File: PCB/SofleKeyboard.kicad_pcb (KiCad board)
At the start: 2 copper layers, 137.2 x 109.2 mm, 87 parts, among them J1 LED, J2 4PIN, J3 OLED, P1 i2c_pin, P2 i2c_pin, SW1 SW_PUSH, SW10 SW_PUSH, SW11 SW_PUSH, SW12 SW_PUSH, SW13 SW_PUSH, SW14 SW_PUSH, SW15 SW_PUSH, SW16 SW_PUSH, SW17 SW_PUSH, SW18 SW_PUSH, SW19 SW_PUSH, SW2 SW_PUSH, SW20 SW_PUSH, SW21 SW_PUSH, SW22 SW_PUSH, SW23 SW_PUSH, SW24 SW_PUSH, SW25 Rotary_Encoder_Switch, SW26 SW_PUSH, SW27 SW_PUSH, SW28 SW_PUSH, SW29 SW_PUSH, SW3 SW_PUSH, SW30 SW_PUSH, SW4 SW_PUSH, SW5 SW_PUSH, SW6 SW_PUSH, SW7 SW_PUSH, SW8 SW_PUSH, SW9 SW_PUSH, U1 ProMicro

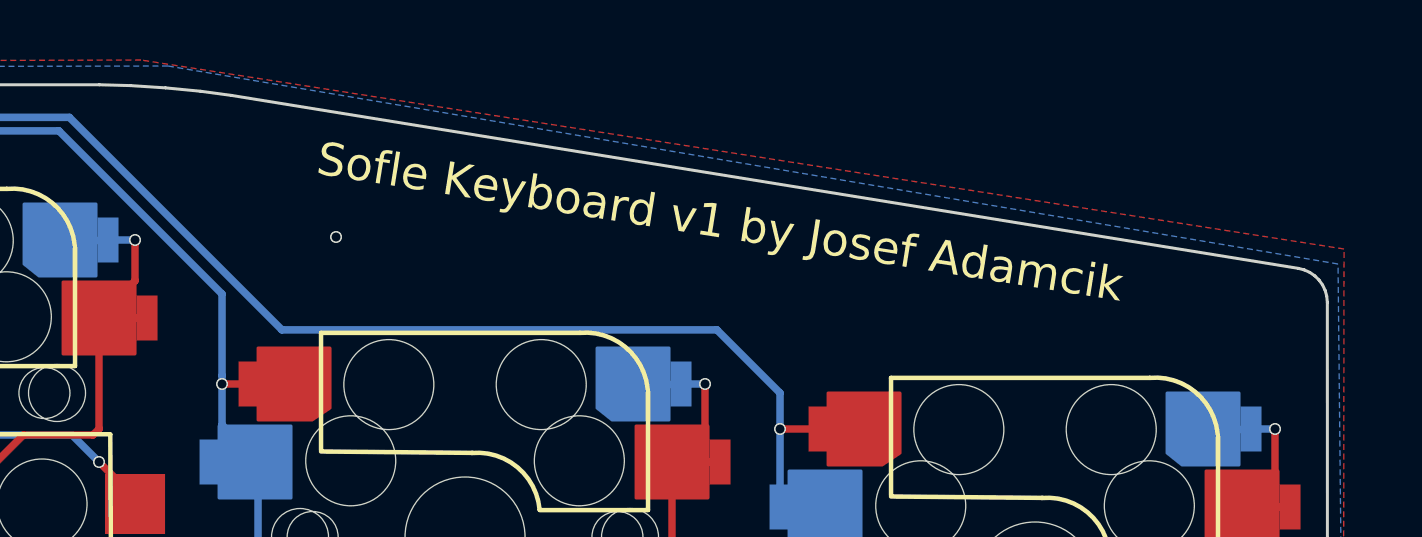
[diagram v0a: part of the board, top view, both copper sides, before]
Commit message: Changed labels on silk screens
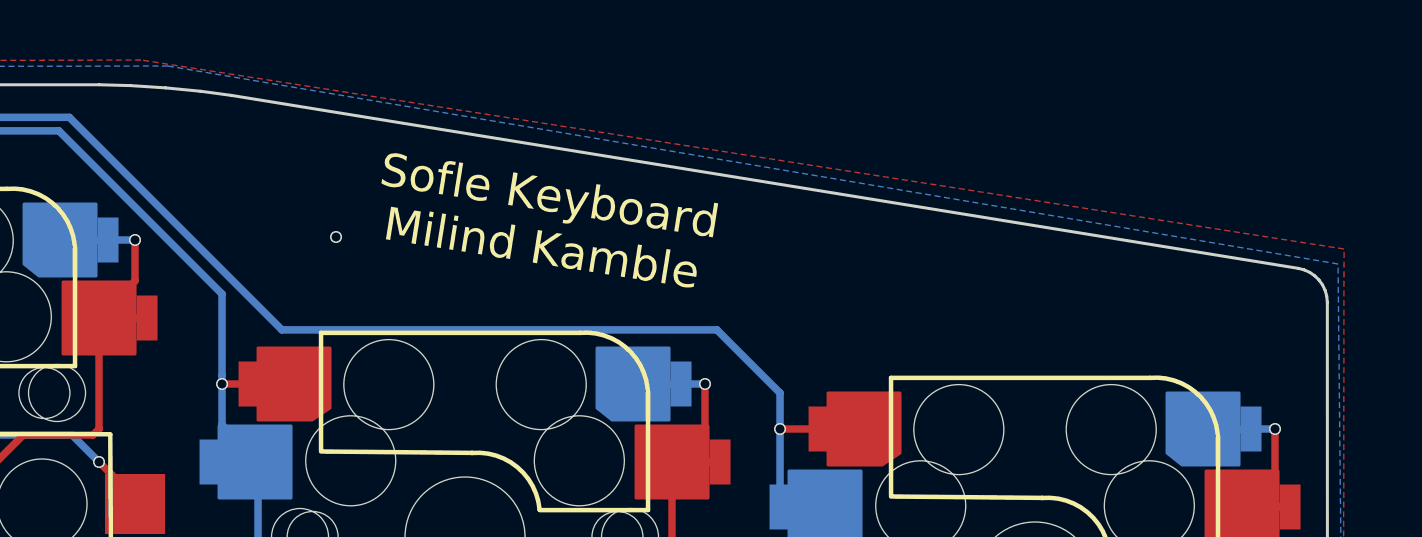
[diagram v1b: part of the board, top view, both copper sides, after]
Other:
- board text added: "Sofle Keyboard Milind Kamble"
- board text removed: "Sofle Keyboard v1 by Josef Adamcik"
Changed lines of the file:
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@@
-(kicad_pcb (version 20171130) (host pcbnew 5.1.4-e60b266~84~ubuntu19.04.1)
+(kicad_pcb (version 20171130) (host pcbnew 5.1.4-e60b266~84~ubuntu18.04.1)
   (general
     (thickness 1.6)
@@
   (page A4)
   (layers
-    (0 F.Cu signal)
-    (31 B.Cu signal)
-    (32 B.Adhes user)
-    (33 F.Adhes user)
-    (34 B.Paste user)
-    (35 F.Paste user)
+    (0 F.Cu signal hide)
+    (31 B.Cu signal hide)
+    (32 B.Adhes user hide)
+    (33 F.Adhes user hide)
+    (34 B.Paste user hide)
+    (35 F.Paste user hide)
     (36 B.SilkS user)
     (37 F.SilkS user)
-    (38 B.Mask user)
-    (39 F.Mask user)
-    (40 Dwgs.User user)
-    (41 Cmts.User user)
-    (42 Eco1.User user)
-    (43 Eco2.User user)
+    (38 B.Mask user hide)
+    (39 F.Mask user hide)
+    (40 Dwgs.User user hide)
+    (41 Cmts.User user hide)
+    (42 Eco1.User user hide)
+    (43 Eco2.User user hide)
     (44 Edge.Cuts user)
-    (45 Margin user)
-    (46 B.CrtYd user)
-    (47 F.CrtYd user)
-    (48 B.Fab user)
-    (49 F.Fab user)
+    (45 Margin user hide)
+    (46 B.CrtYd user hide)
+    (47 F.CrtYd user hide)
+    (48 B.Fab user hide)
+    (49 F.Fab user hide)
   )
   (setup
@@
   (gr_line (start 88.784351 117.684879) (end 88.655972 117.390562) (layer Cmts.User) (width 0.1))
   (gr_line (start 138.11 133.67) (end 106.031074 146.510929) (layer Cmts.User) (width 0.1))
-  (gr_text "Sofle Keyboard v1 by Josef Adamcik" (at 205.1 41.9 -9) (layer B.SilkS)
+  (gr_text "Sofle Keyboard\nMilind Kamble" (at 199.39 41.91 -9) (layer B.SilkS)
     (effects (font (size 1.1 1.1) (thickness 0.2)) (justify mirror))
   )
-  (gr_text "Sofle Keyboard v1 by Josef Adamcik" (at 205.2 41.9 -9) (layer F.SilkS)
+  (gr_text "Sofle Keyboard\nMilind Kamble" (at 199.39 41.91 -9) (layer F.SilkS)
     (effects (font (size 1.1 1.1) (thickness 0.2)))
   )
